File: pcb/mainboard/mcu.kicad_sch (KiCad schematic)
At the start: 26 parts, among them J5 SM03B-SRSS-TB, SW1 SW, SW2 SW, U13 W25Q32JV, U14 RP2040, Y2 12MHz

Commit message: R0P9 PCB WIP
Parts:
- removed J5: SM03B-SRSS-TB, Connector_JST:JST_SH_SM03B-SRSS-TB_1x03-1MP_P1.00mm_Horizontal, symbol Connector_Generic_MountingPin:Conn_01x03_MountingPin
- added J6: Conn_01x08_MountingPin, Connector_FFC-FPC:Hirose_FH12-8S-0.5SH_1x08-1MP_P0.50mm_Horizontal, symbol Connector_Generic_MountingPin:Conn_01x08_MountingPin
- added JP1: Jumper_2_Open, Jumper:SolderJumper-2_P1.3mm_Open_RoundedPad1.0x1.5mm, symbol Jumper:Jumper_2_Open
- added R67: 1K/1%, Resistor_SMD:R_0402_1005Metric, symbol Device:R
- added R68, R69: 5.1K, Resistor_SMD:R_0402_1005Metric, symbol Device:R
- R57: value 1K -> 1K/1%
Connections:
- net +3V3: now also J6.3 (Pin_3), R68.1, R69.1
- net GND: now also J6.8 (Pin_8), J6.MP (MountPin), JP1.1 (A)
- net I2C_SCL: now also R69.2
- net I2C_SDA: now also R68.2
- net QSPI_SS: now also R67.2
- net SWCLK: now also J6.1 (Pin_1)
- net SWD: now also J6.2 (Pin_2)
- net FL_PWM renamed GPIO16
- net GPIO23 renamed FL_PWM1
- net GPIO24 renamed FL_PWM2
- new net: JP1.2 (B), R67.1
- new net FPGA_TCK: J6.7 (Pin_7)
- new net FPGA_TDI: J6.4 (Pin_4)
- new net FPGA_TDO: J6.5 (Pin_5)
- new net FPGA_TMS: J6.6 (Pin_6)

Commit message: PCB r0p9
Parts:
- removed C100, C101, C156, C90, C91, C94, C95, C96, C97, C98, C99: 100nF, Capacitor_SMD:C_0402_1005Metric, symbol Device:C
- removed C102, C89: 1uF, Capacitor_SMD:C_0402_1005Metric, symbol Device:C
- removed C92, C93: 18pF, Capacitor_SMD:C_0402_1005Metric, symbol Device:C
- removed J6: Conn_01x08_MountingPin, Connector_FFC-FPC:Hirose_FH12-8S-0.5SH_1x08-1MP_P0.50mm_Horizontal, symbol Connector_Generic_MountingPin:Conn_01x08_MountingPin
- removed JP1: Jumper_2_Open, Jumper:SolderJumper-2_P1.3mm_Open_RoundedPad1.0x1.5mm, symbol Jumper:Jumper_2_Open
- removed R50, R51: 1M, Resistor_SMD:R_0402_1005Metric, symbol Device:R
- removed R57, R67: 1K/1%, Resistor_SMD:R_0402_1005Metric, symbol Device:R
- removed R58, R59: 27R, Resistor_SMD:R_0402_1005Metric, symbol Device:R
- removed R68, R69: 5.1K, Resistor_SMD:R_0402_1005Metric, symbol Device:R
- removed SW1, SW2: SW, Button_Switch_SMD:Panasonic_EVQPUL_EVQPUC, symbol Switch:SW_Push
- removed U13: W25Q32JV, Package_SON:WSON-8-1EP_6x5mm_P1.27mm_EP3.4x4.3mm, symbol Memory_Flash:W25Q32JVZP
- removed U14: RP2040, footprints:RP2040-QFN-56, symbol MCU_RaspberryPi:RP2040
- removed Y2: 12MHz, Crystal:Crystal_SMD_3225-4Pin_3.2x2.5mm, symbol Device:Crystal_GND24

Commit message: PCB r0p10 wip
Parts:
- added C214: 22uF, Capacitor_SMD:C_0603_1608Metric, symbol Device:C
- added C215: 100nF, Capacitor_SMD:C_0402_1005Metric, symbol Device:C
- added D19: LED GREEN, LED_SMD:LED_0603_1608Metric, symbol Device:LED
- added D20: LED RED, LED_SMD:LED_0603_1608Metric, symbol Device:LED
- added J7: MICRO_SD(TFC-WPAPR-08), footprints:TFC-WPAPR-08, symbol symbols:MICRO_SD(TFC-WPAPR-08)
- added R12, R14: 10K, Resistor_SMD:R_0402_1005Metric, symbol Device:R
- added R42, R43: 1K, Resistor_SMD:R_0402_1005Metric, symbol Device:R
- added SW1, SW2: SW, Button_Switch_SMD:Panasonic_EVQPUL_EVQPUC, symbol Switch:SW_Push
- added U14: STM32F407VGTx, Package_QFP:LQFP-100_14x14mm_P0.5mm, symbol MCU_ST_STM32F4:STM32F407VGTx
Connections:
- new net: D20.2 (A), R43.2
- new net: D19.2 (A), R42.2
- new net: U14.10 (VSS), U14.27 (VSS), U14.74 (VSS), U14.99 (VSS)
- new net +3V3: C214.1, C215.1, J7.4 (VDD), R12.1, R14.1
- new net EPD_VCOM_PWM: U14.67 (PA8)
- new net FL_PWM1: U14.42 (PE11)
- new net FL_PWM2: U14.44 (PE13)
- new net FPGA_CS: U14.77 (PA15)
- new net FPGA_MISO: U14.90 (PB4)
- new net FPGA_MOSI: U14.91 (PB5)
- new net FPGA_SCLK: U14.89 (PB3)
- new net FSMC_A16: U14.58 (PD11)
- new net FSMC_D0: U14.61 (PD14)
- new net FSMC_D1: U14.62 (PD15)
- new net FSMC_D2: U14.81 (PD0)
- new net FSMC_D3: U14.82 (PD1)
- new net FSMC_D4: U14.38 (PE7)
- new net FSMC_D5: U14.39 (PE8)
- new net FSMC_D6: U14.40 (PE9)
- new net FSMC_D7: U14.41 (PE10)
- new net FSMC_NE1: U14.88 (PD7)
- new net FSMC_NOE: U14.85 (PD4)
- new net FSMC_NWE: U14.86 (PD5)
- new net GND: C214.2, C215.2, D19.1 (K), D20.1 (K), J7.10, J7.11, J7.12, J7.13, J7.6 (VSS), SW1.2, SW2.2
- new net G_LED: R42.1
- new net I2C1_SCL: R14.2, U14.92 (PB6)
- new net I2C1_SDA: R12.2, U14.93 (PB7)
- new net KEY1: SW2.1
- new net KEY2: SW1.1
- new net MCU_SWCLK: U14.76 (PA14)
- new net MCU_SWDIO: U14.72 (PA13)
- new net R_LED: R43.1
- new net SDIO_CLK: J7.5 (CLK/SCLK), U14.80 (PC12)
- new net SDIO_CMD: J7.3 (CMD/DI), U14.83 (PD2)
- new net SDIO_DAT0: J7.7 (DAT0/DO), U14.65 (PC8)
- new net SDIO_DAT1: J7.8 (DAT1/RES), U14.66 (PC9)
- new net SDIO_DAT2: J7.1 (DAT2/RES), U14.78 (PC10)
- new net SDIO_DAT3: J7.2 (CD/DAT3/CS), U14.79 (PC11)
- new net USB_DN: U14.70 (PA11)
- new net USB_DP: U14.71 (PA12)
- new net VBUS_MEA: U14.36 (PB1)
- new net VCOM_MEA: U14.35 (PB0)
- new net VGH_MEA: U14.26 (PA3)
- new net VGL_MEA: U14.32 (PA7)
- new net VN1_MEA: U14.29 (PA4)
- new net VN2_MEA: U14.30 (PA5)
- new net VN3_MEA: U14.31 (PA6)
- new net VP1_MEA: U14.23 (PA0)
- new net VP2_MEA: U14.24 (PA1)
- new net VP3_MEA: U14.25 (PA2)
- no-connect marks 0 -> 2

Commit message: PCB r0p10
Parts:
- removed U14: STM32F407VGTx, Package_QFP:LQFP-100_14x14mm_P0.5mm, symbol MCU_ST_STM32F4:STM32F407VGTx
- added C10, C13, C28, C6: 18pF, Capacitor_SMD:C_0402_1005Metric, symbol Device:C
- added C145, C146, C34, C47: 4.7uF, Capacitor_SMD:C_0402_1005Metric, symbol Device:C
- added C29, C3, C30, C31, C36, C39, C40, C43, C48, C50: 100nF, Capacitor_SMD:C_0402_1005Metric, symbol Device:C
- added C89, C90: 2.2uF, Capacitor_SMD:C_0402_1005Metric, symbol Device:C
- added FB3: 120R, Inductor_SMD:L_0603_1608Metric, symbol Device:FerriteBead
- added J5: 02x16_1.27_HDR, Connector_PinSocket_1.27mm:PinSocket_2x06_P1.27mm_Vertical_SMD, symbol Connector_Generic:Conn_02x06_Odd_Even
- added R20: 1K, Resistor_SMD:R_0402_1005Metric, symbol Device:R
- added R21: 10K, Resistor_SMD:R_0402_1005Metric, symbol Device:R
- added U14: W25Q32JV, Package_SON:WSON-8-1EP_6x5mm_P1.27mm_EP3.4x4.3mm, symbol Memory_Flash:W25Q32JVZP
- added U3: STM32H750VBTx, Package_QFP:LQFP-100_14x14mm_P0.5mm, symbol MCU_ST_STM32H7:STM32H750VBTx
- added Y1: 24MHz, Crystal:Crystal_SMD_3225-4Pin_3.2x2.5mm, symbol Device:Crystal_GND24
- added Y2: 32.768K, Crystal:Crystal_SMD_TXC_9HT11-2Pin_2.0x1.2mm_HandSoldering, symbol Device:Crystal
- C214: value 22uF -> 47uF/6.3V
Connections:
- net +3V3: now also SW1.2, SW2.2, C3.1, C30.1, C31.1, C34.1, C36.1, C39.1, C40.1, C43.1, FB3.1, J5.12 (Pin_12), U14.8 (VCC), U3.100 (VDD), U3.11 (VDD), U3.27 (VDD), U3.50 (VDD), U3.6 (VBAT), U3.75 (VDD)
- net DEC_RST: now also U3.87 (PD6)
- net DP_HPD: now also U3.88 (PD7)
- net DP_PDN: now also U3.84 (PD3)
- net EPD_PWR_EN: now also U3.41 (PE11)
- net EPD_SHDN: now also U3.42 (PE12)
- net EPD_THROT: now also U3.83 (PD2)
- net FL_PWM1: now also U3.43 (PE13)
- net FL_PWM2: now also U3.44 (PE14)
- net FPGA_CS: now also U3.51 (PB12)
- net FPGA_DONE: now also U3.79 (PC11)
- net FPGA_MISO: now also U3.17 (PC2_C)
- net FPGA_MOSI: now also U3.18 (PC3_C)
- net FPGA_PROG: now also U3.78 (PC10)
- net FPGA_SCLK: now also U3.52 (PB13)
- net FPGA_SUSP: now also U3.80 (PC12)
- net GND: now also C10.2, C13.2, C145.1, C146.1, C28.2, C29.1, C3.2, C30.2, C31.2, C34.2, C36.2, C39.2, C40.2, C43.2, C47.2, C48.2, C50.2, C6.2, C89.1, C90.1, J5.10 (Pin_10), J5.2 (Pin_2), J5.4 (Pin_4), J5.6 (Pin_6), J5.8 (Pin_8), R21.1, U14.4 (GND), U14.9 (EP), U3.10 (VSS), U3.19 (VSSA), U3.26 (VSS), U3.49 (VSS), U3.74 (VSS), U3.99 (VSS), Y1.2, Y1.4; no longer SW1.2, SW2.2
- net G_LED: now also U3.97 (PE0)
- net I2C1_SCL: now also U3.92 (PB6)
- net I2C1_SDA: now also U3.93 (PB7)
- net KEY1: now also R21.2, U3.94 (BOOT0)
- net KEY2: now also U3.91 (PB5)
- net MCU_SWCLK: now also J5.9 (Pin_9), U3.76 (PA14)
- net MCU_SWDIO: now also J5.11 (Pin_11), U3.72 (PA13)
- net R_LED: now also U3.98 (PE1)
- net SDIO_CLK: now also U3.16 (PC1)
- net SDIO_CMD: now also U3.22 (PA0)
- net SDIO_DAT0: now also U3.53 (PB14)
- net SDIO_DAT1: now also U3.54 (PB15)
- net SDIO_DAT2: now also U3.89 (PB3)
- net SDIO_DAT3: now also U3.90 (PB4)
- net TCPC_INT: now also U3.77 (PA15)
- net TYPEC_ORI: now also U3.69 (PA10)
- net USB_DN: now also U3.70 (PA11)
- net USB_DP: now also U3.71 (PA12)
- net VBUS_MEA: now also U3.35 (PB1)
- net VCOM_EN: now also U3.25 (PA3)
- net VCOM_MEA: now also U3.31 (PA7)
- net VGH_MEA: now also U3.32 (PC4)
- net VGL_MEA: now also U3.34 (PB0)
- new net: C145.2, C146.2, C89.2, C90.2, U3.48 (VCAP), U3.73 (VCAP)
- new net: C10.1, R20.2, Y1.3
- new net: C29.2, U3.14 (NRST)
- new net +3V3A: C47.1, C48.1, C50.1, FB3.2, U3.20 (VREF+), U3.21 (VDDA)
- new net FL_EN: U3.45 (PE15)
- new net FMC_A16: U3.58 (PD11)
- new net FMC_D0: U3.61 (PD14)
- new net FMC_D1: U3.62 (PD15)
- new net FMC_D2: U3.81 (PD0)
- new net FMC_D3: U3.82 (PD1)
- new net FMC_D4: U3.37 (PE7)
- new net FMC_D5: U3.38 (PE8)
- new net FMC_D6: U3.39 (PE9)
- new net FMC_D7: U3.40 (PE10)
- new net FMC_NE1: U3.64 (PC7)
- new net FMC_NOE: U3.85 (PD4)
- new net FMC_NWE: U3.86 (PD5)
- new net FPGA_TCK: J5.1 (Pin_1)
- new net FPGA_TDI: J5.3 (Pin_3)
- new net FPGA_TDO: J5.5 (Pin_5)
- new net FPGA_TMS: J5.7 (Pin_7)
- new net OSC32_IN: C13.1, U3.8 (PC14), Y2.1
- new net OSC32_OUT: C28.1, U3.9 (PC15), Y2.2
- new net OSC_IN: C6.1, U3.12 (PH0), Y1.1
- new net OSC_OUT: R20.1, U3.13 (PH1)
- new net QSPI_SCLK: U14.6 (CLK), U3.36 (PB2)
- new net QSPI_SD0: U14.5 (DI(IO0)), U3.66 (PC9)
- new net QSPI_SD1: U14.2 (DO(IO1)), U3.59 (PD12)
- new net QSPI_SD2: U14.3 (IO2), U3.1 (PE2)
- new net QSPI_SD3: U14.7 (IO3), U3.23 (PA1)
- new net QSPI_SS: U14.1 (~{CS}), U3.46 (PB10)
- new net VCOM_DAC: U3.28 (PA4)
- new net VCOM_MEA_EN: U3.24 (PA2)
- new net VGH_DAC: U3.29 (PA5)
- new net VN_MEA: U3.33 (PC5)
- new net VP_MEA: U3.30 (PA6)
- no-connect marks 2 -> 1
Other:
- moved on the sheet: C214, C215, J7, R12, R14, SW1, SW2

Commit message: PCB r0p13
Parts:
- added SW3: SW, Button_Switch_SMD:Panasonic_EVQPUL_EVQPUC, symbol Switch:SW_Push
- C10, C13, C28, C6: value 18pF -> 18pF/50V
- C145, C146, C34, C47: value 4.7uF -> 4.7uF/6.3V
- C214: value 47uF/6.3V -> 22uF/6.3V
- C215, C29, C3, C30, C31, C36, C39, C40, C43, C48, C50: value 100nF -> 100nF/50V
- C89, C90: value 2.2uF -> 4.7uF/6.3V
- FB3: value 120R -> 120R@100M
- R12, R14, R21: value 10K -> 10K/1%
- R20, R43: value 1K -> 1K/1%
- R42: value 1K -> 10K/1%
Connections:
- net +3V3: now also SW3.2
- net KEY1: now also SW1.1, U3.3 (PE4); no longer SW2.1
- net KEY2: now also SW2.1; no longer SW1.1
- net KEY3: now reaches U3.2 (PE3)
- net KEY3: now also SW3.1
- net USER_PD8: now reaches U3.55 (PD8)
- net USER_PD9: now reaches U3.56 (PD9)
- net USER_PD10: now reaches U3.57 (PD10)
- net USER_PD13: now reaches U3.60 (PD13)
- net USER_PB8: now reaches U3.95 (PB8)
- net USER_PB9: now reaches U3.96 (PB9)
- net EPD_SHDN renamed EPD_POS_EN
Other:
- company: Copyright 2024 Wenting Zhang -> Copyright 2025 Wenting Zhang
- moved on the sheet: SW1, SW2

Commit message: PCB r1.1
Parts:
- C10, C13, C28, C6: LCSC (none) -> C106202
- C145, C146, C34, C47, C89, C90: LCSC (none) -> C307423
- C214: LCSC (none) -> C59461
- C215, C29, C3, C30, C31, C36, C39, C40, C43, C48, C50: LCSC (none) -> C131394
- D19: LCSC (none) -> C965804
- D20: LCSC (none) -> C965799
- FB3: LCSC (none) -> C14709
- J5: value 02x16_1.27_HDR -> 2x6_1.27_HDR; LCSC (none) -> C3975132
- J7: LCSC (none) -> C91145
- R12, R14, R21, R42: LCSC (none) -> C25744
- R20, R43: LCSC (none) -> C11702
- SW1, SW2, SW3: LCSC (none) -> C79174
- U14: LCSC (none) -> C571260
- U3: LCSC (none) -> C404010
- Y1: LCSC (none) -> C70590
- Y2: LCSC (none) -> C7500573
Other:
- company: Copyright 2025 Wenting Zhang -> Copyright 2025 Modos Tech Inc

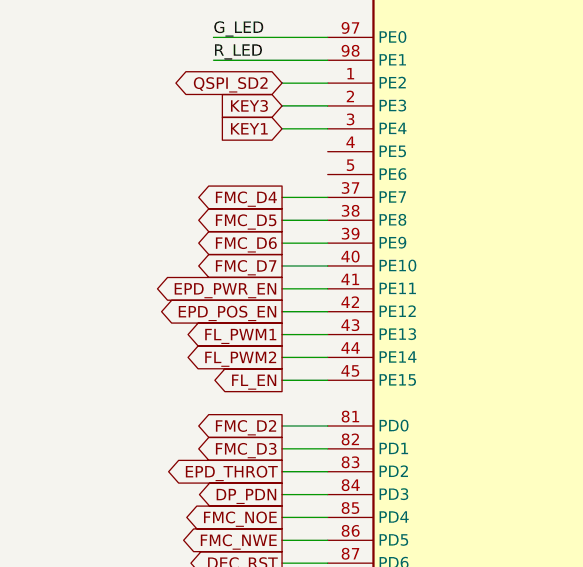
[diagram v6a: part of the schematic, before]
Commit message: PCB r1.2, new adapters
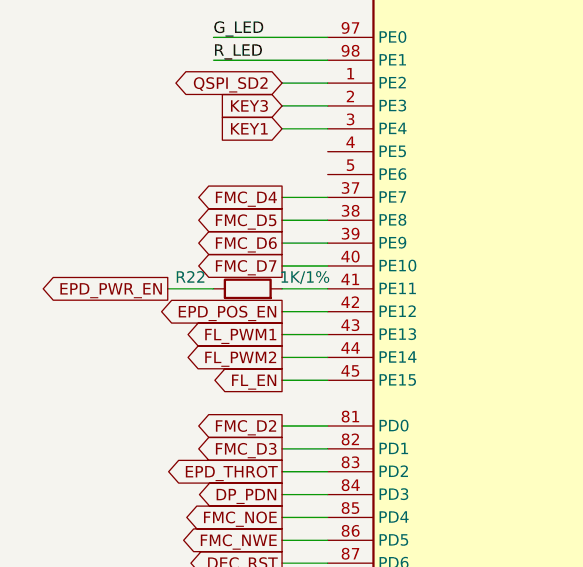
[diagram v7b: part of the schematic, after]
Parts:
- added R22: 1K/1%, Resistor_SMD:R_0402_1005Metric, symbol Device:R
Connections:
- net EPD_PWR_EN: now also R22.1; no longer U3.41 (PE11)
- new net: R22.2, U3.41 (PE11)
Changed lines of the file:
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@@
 	(wire
 		(pts
+			(xy 27.94 88.9) (xy 33.02 88.9)
+		)
+		(stroke
+			(width 0)
+			(type default)
+		)
+	)
+	(wire
+		(pts
 			(xy 215.9 33.02) (xy 228.6 33.02)
 		)
@@
 	(wire
 		(pts
+			(xy 40.64 88.9) (xy 45.72 88.9)
+		)
+		(stroke
+			(width 0)
+			(type default)
+		)
+	)
+	(wire
+		(pts
 			(xy 124.46 33.02) (xy 137.16 33.02)
 		)
@@
 	(wire
 		(pts
-			(xy 45.72 88.9) (xy 40.64 88.9)
-		)
-		(stroke
-			(width 0)
-			(type default)
-		)
-	)
-	(wire
-		(pts
 			(xy 40.64 142.24) (xy 45.72 142.24)
 		)
@@
 	(global_label "EPD_PWR_EN"
 		(shape output)
-		(at 40.64 88.9 180)
+		(at 27.94 88.9 180)
 		(effects
 			(font
@@
 		)
 		(property "Intersheetrefs" "${INTERSHEET_REFS}"
-			(at -63.5 -25.4 0)
+			(at -76.2 -25.4 0)
 			(effects
 				(font
@@
 					(unit 1)
 				)
+			)
+		)
+	)
+	(symbol
+		(lib_id "Device:R")
+		(at 36.83 88.9 90)
+		(unit 1)
+		(exclude_from_sim no)
+		(in_bom yes)
+		(on_board yes)
+		(dnp no)
+		(property "Reference" "R22"
+			(at 30.48 87.63 90)
+			(effects
+				(font
+					(size 1.27 1.27)
+				)
+			)
+		)
+		(property "Value" "1K/1%"
+			(at 43.18 87.63 90)
+			(effects
+				(font
+					(size 1.27 1.27)
+				)
+			)
+		)
+		(property "Footprint" "Resistor_SMD:R_0402_1005Metric"
+			(at 36.83 90.678 90)
+			(effects
+				(font
+					(size 1.27 1.27)
+				)
+				(hide yes)
+			)
+		)
+		(property "Datasheet" "~"
+			(at 36.83 88.9 0)
+			(effects
+				(font
+					(size 1.27 1.27)
+				)
+				(hide yes)
+			)
+		)
+		(property "Description" ""
+			(at 36.83 88.9 0)
+			(effects
+				(font
+					(size 1.27 1.27)
+				)
+				(hide yes)
+			)
+		)
+		(property "desc" ""
+			(at 36.83 88.9 0)
+			(effects
+				(font
+					(size 1.27 1.27)
+				)
+				(hide yes)
+			)
+		)
+		(property "LCSC" "C11702"
+			(at 36.83 88.9 0)
+			(effects
+				(font
+					(size 1.27 1.27)
+				)
+				(hide yes)
+			)
+		)
+		(pin "1"
+		)
+		(pin "2"
+		)
+		(instances
+			(project "pcb"
+				(path "/4654897e-3e2f-4522-96c3-20b19803c088/5f589a85-47ef-4b9c-90f9-dfdcb1c7f590"
+					(reference "R22")
+					(unit 1)
+				)
